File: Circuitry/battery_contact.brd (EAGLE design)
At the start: 20 x 20 mm, 2 parts

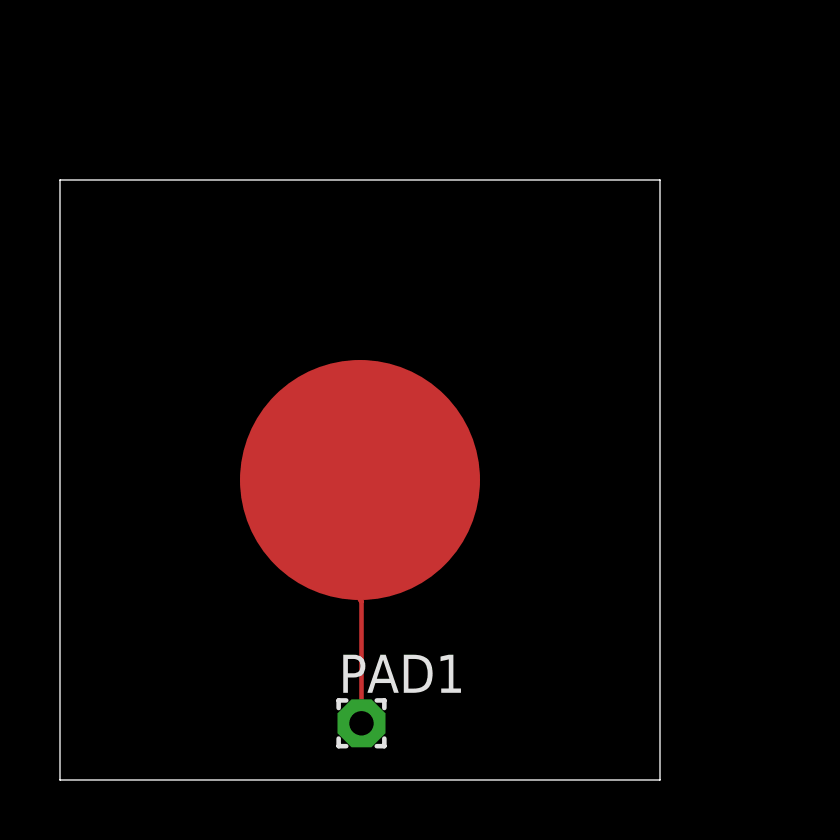
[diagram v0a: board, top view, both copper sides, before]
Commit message: adjust board dimensions
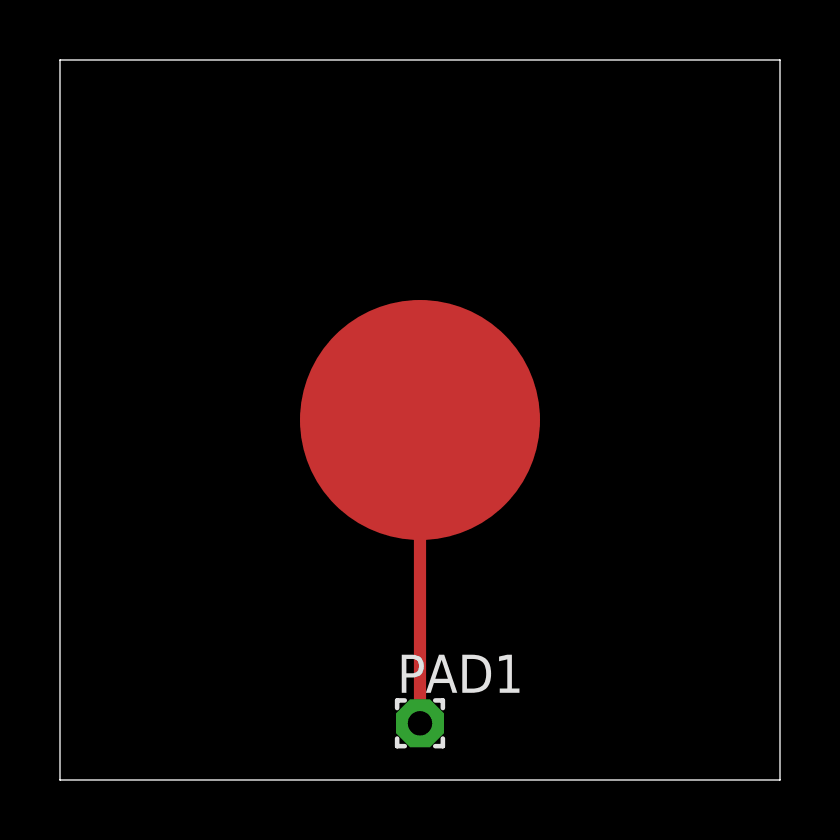
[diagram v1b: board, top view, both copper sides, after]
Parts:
- moved U$1 2.83 mm to (12.0, 12.0)
- moved PAD1 1.95 mm to (12.0, 1.89)
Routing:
- net N$1: track 4.13 -> 10.1 mm
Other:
- board size 20 x 20 mm -> 24 x 24 mm
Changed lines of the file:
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@@
 <?xml version="1.0" encoding="utf-8"?>
 <!DOCTYPE eagle SYSTEM "eagle.dtd">
-<eagle version="9.5.0">
+<eagle version="9.5.1">
 <drawing>
 <settings>
@@
 <setting verticaltext="up"/>
 </settings>
-<grid distance="0.25" unitdist="mm" unit="mm" style="lines" multiple="1" display="no" altdistance="5" altunitdist="mil" altunit="mil"/>
+<grid distance="1" unitdist="mm" unit="mm" style="lines" multiple="1" display="no" altdistance="5" altunitdist="mil" altunit="mil"/>
 <layers>
 <layer number="1" name="Top" color="4" fill="1" visible="yes" active="yes"/>
@@
 <board>
 <plain>
-<wire x1="0" y1="0" x2="20" y2="0" width="0" layer="20"/>
-<wire x1="20" y1="0" x2="20" y2="20" width="0" layer="20"/>
-<wire x1="20" y1="20" x2="0" y2="20" width="0" layer="20"/>
-<wire x1="0" y1="20" x2="0" y2="0" width="0" layer="20"/>
+<wire x1="0" y1="0" x2="24" y2="0" width="0" layer="20"/>
+<wire x1="24" y1="0" x2="24" y2="24" width="0" layer="20"/>
+<wire x1="24" y1="24" x2="0" y2="24" width="0" layer="20"/>
+<wire x1="0" y1="24" x2="0" y2="0" width="0" layer="20"/>
 </plain>
 <attributes>
@@
 </autorouter>
 <elements>
-<element name="U$1" library="custom_library" package="CONTACT_REGION" value="CONTACT_REGION" x="10" y="10" smashed="yes"/>
-<element name="PAD1" library="wirepad" library_urn="urn:adsk.eagle:library:412" package="1,6/0,8" package3d_urn="urn:adsk.eagle:package:30830/1" value="" x="10.05" y="1.89" smashed="yes">
-<attribute name="NAME" x="9.288" y="2.906" size="1.27" layer="25" ratio="10"/>
-<attribute name="POPULARITY" value="15" x="10.05" y="1.89" size="1.778" layer="27" display="off"/>
-<attribute name="VALUE" x="10.05" y="2.49" size="0.0254" layer="27"/>
+<element name="U$1" library="custom_library" package="CONTACT_REGION" value="CONTACT_REGION" x="12" y="12" smashed="yes"/>
+<element name="PAD1" library="wirepad" library_urn="urn:adsk.eagle:library:412" package="1,6/0,8" package3d_urn="urn:adsk.eagle:package:30830/1" value="" x="12" y="1.89" smashed="yes">
+<attribute name="NAME" x="11.238" y="2.906" size="1.27" layer="25" ratio="10"/>
+<attribute name="POPULARITY" value="15" x="12" y="1.89" size="1.778" layer="27" display="off"/>
+<attribute name="VALUE" x="12" y="2.49" size="0.0254" layer="27"/>
 </element>
 </elements>
@@
 <contactref element="U$1" pad="P$1"/>
 <contactref element="PAD1" pad="1"/>
-<wire x1="10.05" y1="1.89" x2="10.05" y2="5.95" width="0.1524" layer="1"/>
-<wire x1="10.05" y1="5.95" x2="10" y2="6" width="0.1524" layer="1"/>
-<wire x1="10" y1="6" x2="10" y2="10" width="0" layer="19" extent="1-1"/>
+<wire x1="12" y1="12" x2="12" y2="1.89" width="0.4064" layer="1"/>
 </signal>
 </signals>
